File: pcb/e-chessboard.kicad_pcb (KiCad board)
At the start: 2 copper layers, 170 x 170 mm, 55 parts, among them J1 POWER, J2 UART, Q1 BC847, Q2 BC847, SW1 Reset, SW2 Boot, U1 ESP32-WROOM-32U, U2 AOZ1280, U3 NCV7608

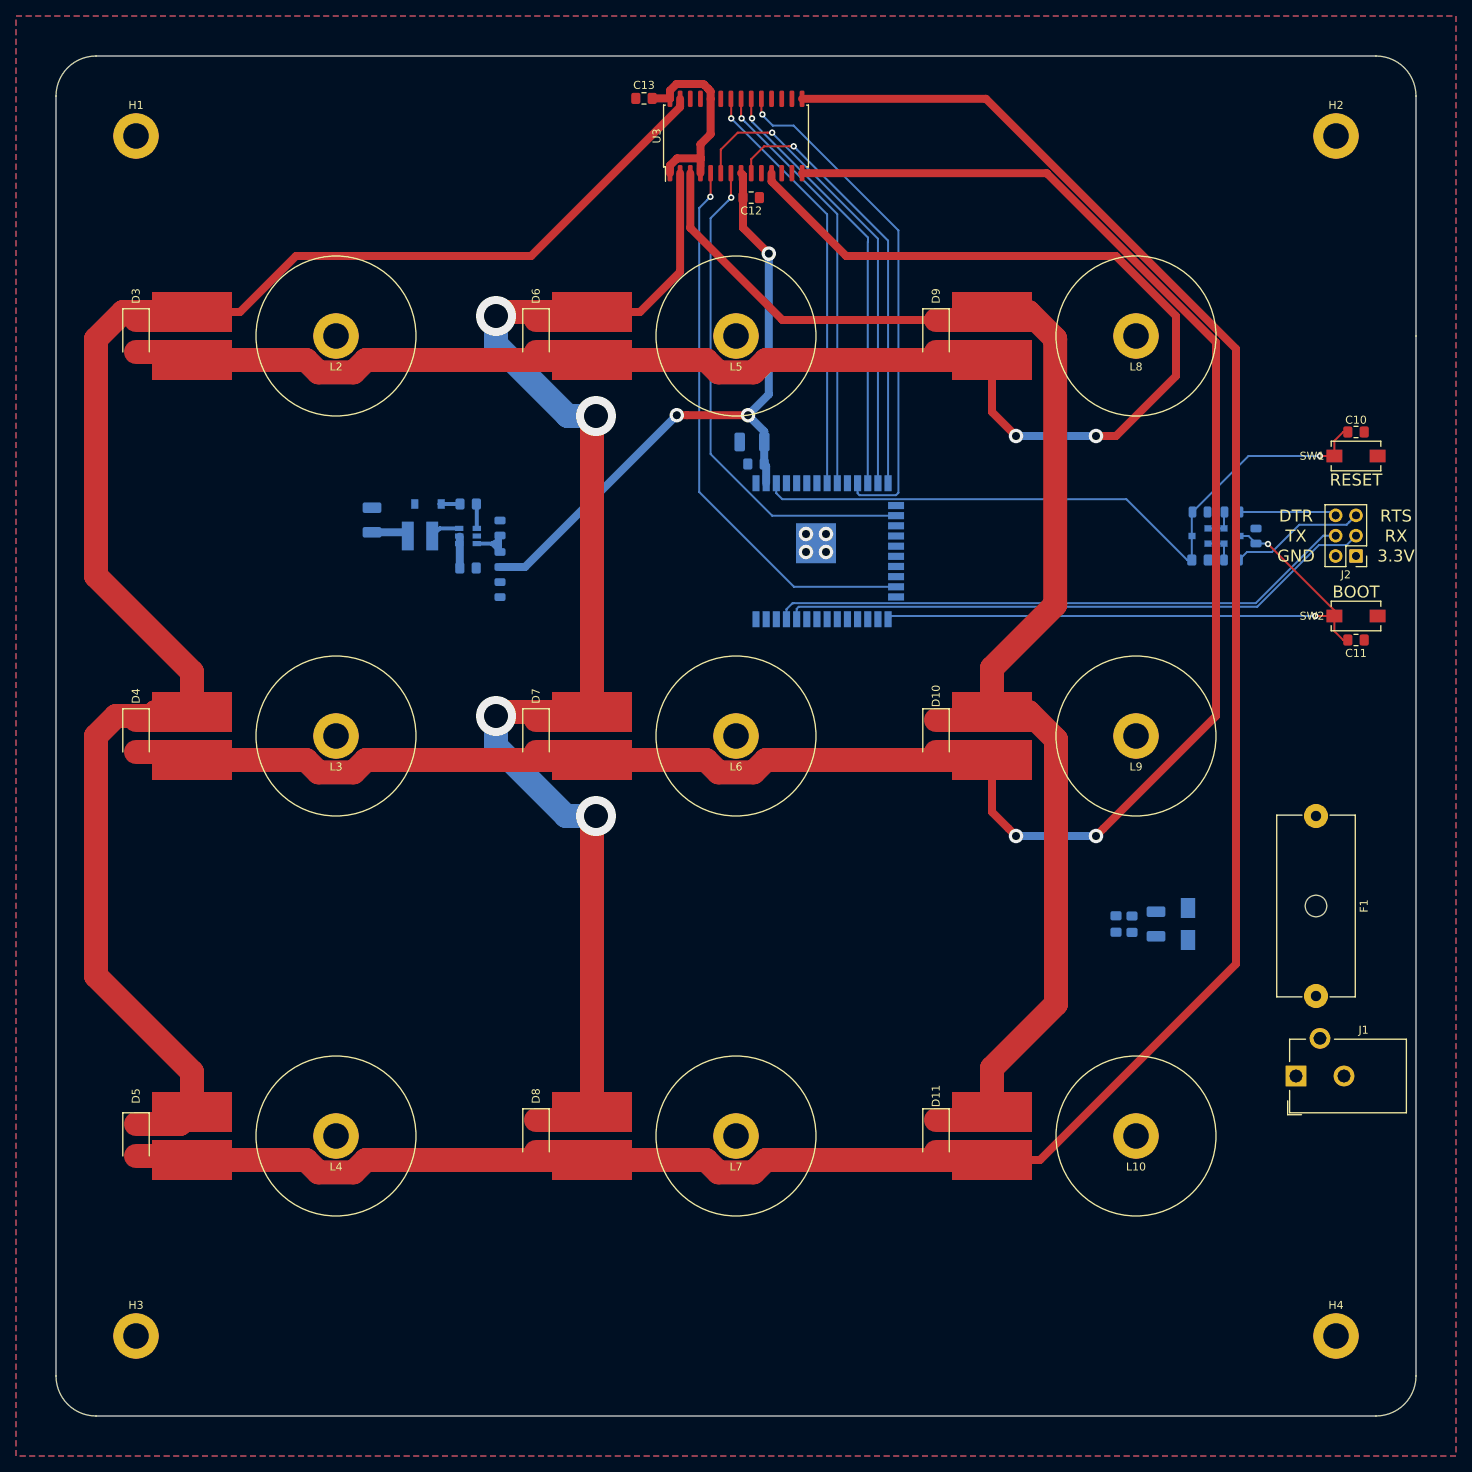
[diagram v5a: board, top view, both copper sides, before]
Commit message: feat(kicad): laying all traces
Laying all missing traces. Next step: via stitching
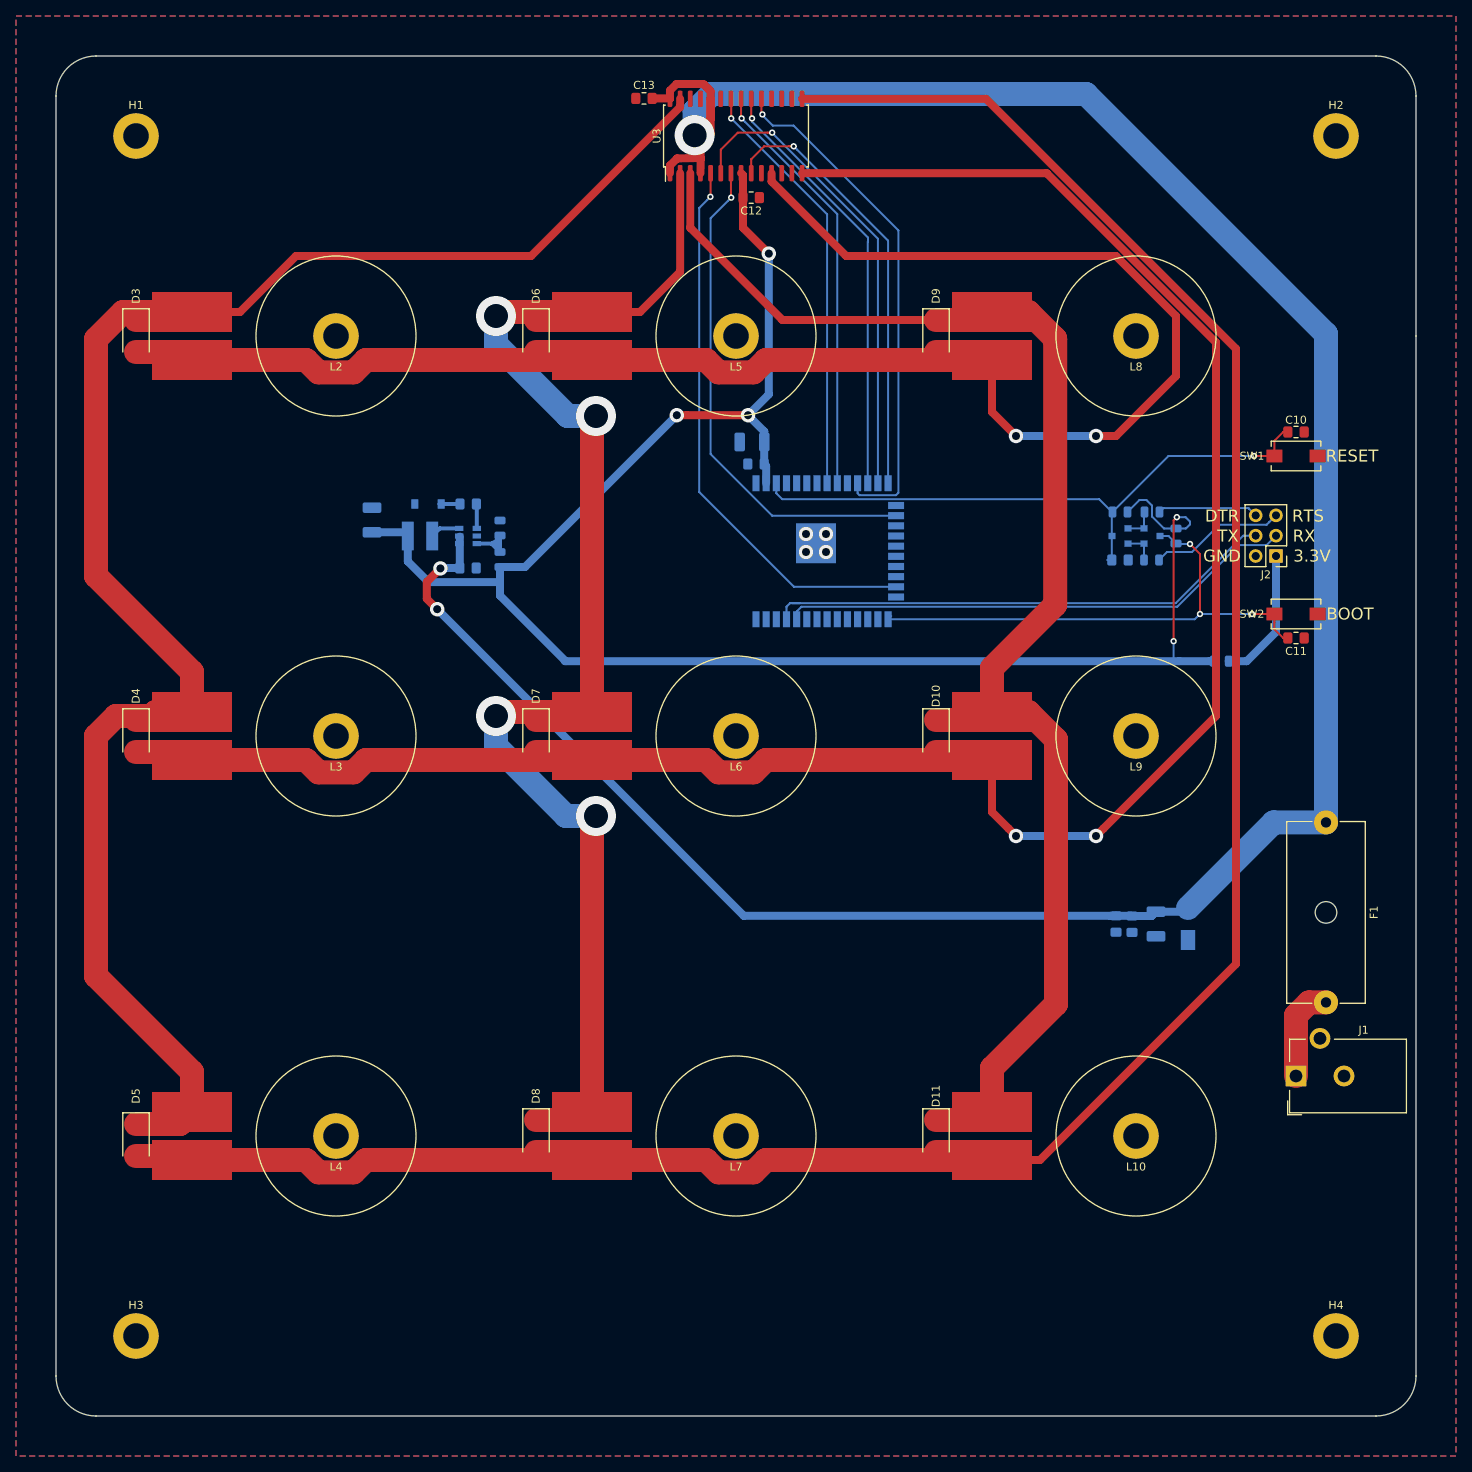
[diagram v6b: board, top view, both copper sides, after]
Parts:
- moved R7 90.6 mm to (195.7, 125.7), turned to 180 degrees
- moved C9 10.0 mm to (183.0, 113.0)
- moved J2 10.0 mm to (202.5, 112.5)
- moved Q1 10.0 mm to (183.0, 110.0)
- moved Q2 10.0 mm to (187.0, 110.0)
- moved R1 10.0 mm to (187.0, 107.0)
- moved R2 10.0 mm to (186.9, 113.0)
- moved R5 10.0 mm to (183.0, 107.0)
- moved R6 10.0 mm to (190.0, 110.0)
- moved C11 7.50 mm to (205.0, 122.8)
- moved SW2 7.50 mm to (205.0, 119.8)
- moved C10 7.50 mm to (205.0, 97.0)
- moved SW1 7.50 mm to (205.0, 100.0)
- moved F1 1.48 mm to (208.8, 145.8)
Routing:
- net +12V: track 33.0 -> 338.4 mm, vias 0 -> 3
- net +3V3: track 85.7 -> 229.1 mm, vias 3 -> 5
- net Net-(J2-Pad1): track 0.00 -> 16.9 mm
- net Net-(F1-Pad2): track 0.00 -> 12.0 mm
- net UART_RX: track 75.0 -> 64.8 mm
- net EN: track 87.3 -> 78.2 mm
- net UART_TX: track 73.7 -> 64.9 mm
- net IO0: track 76.3 -> 71.3 mm, vias 2 -> 3

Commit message: feat(kicad): adding via stictes
Adding 0.8/0.4 via stitching.
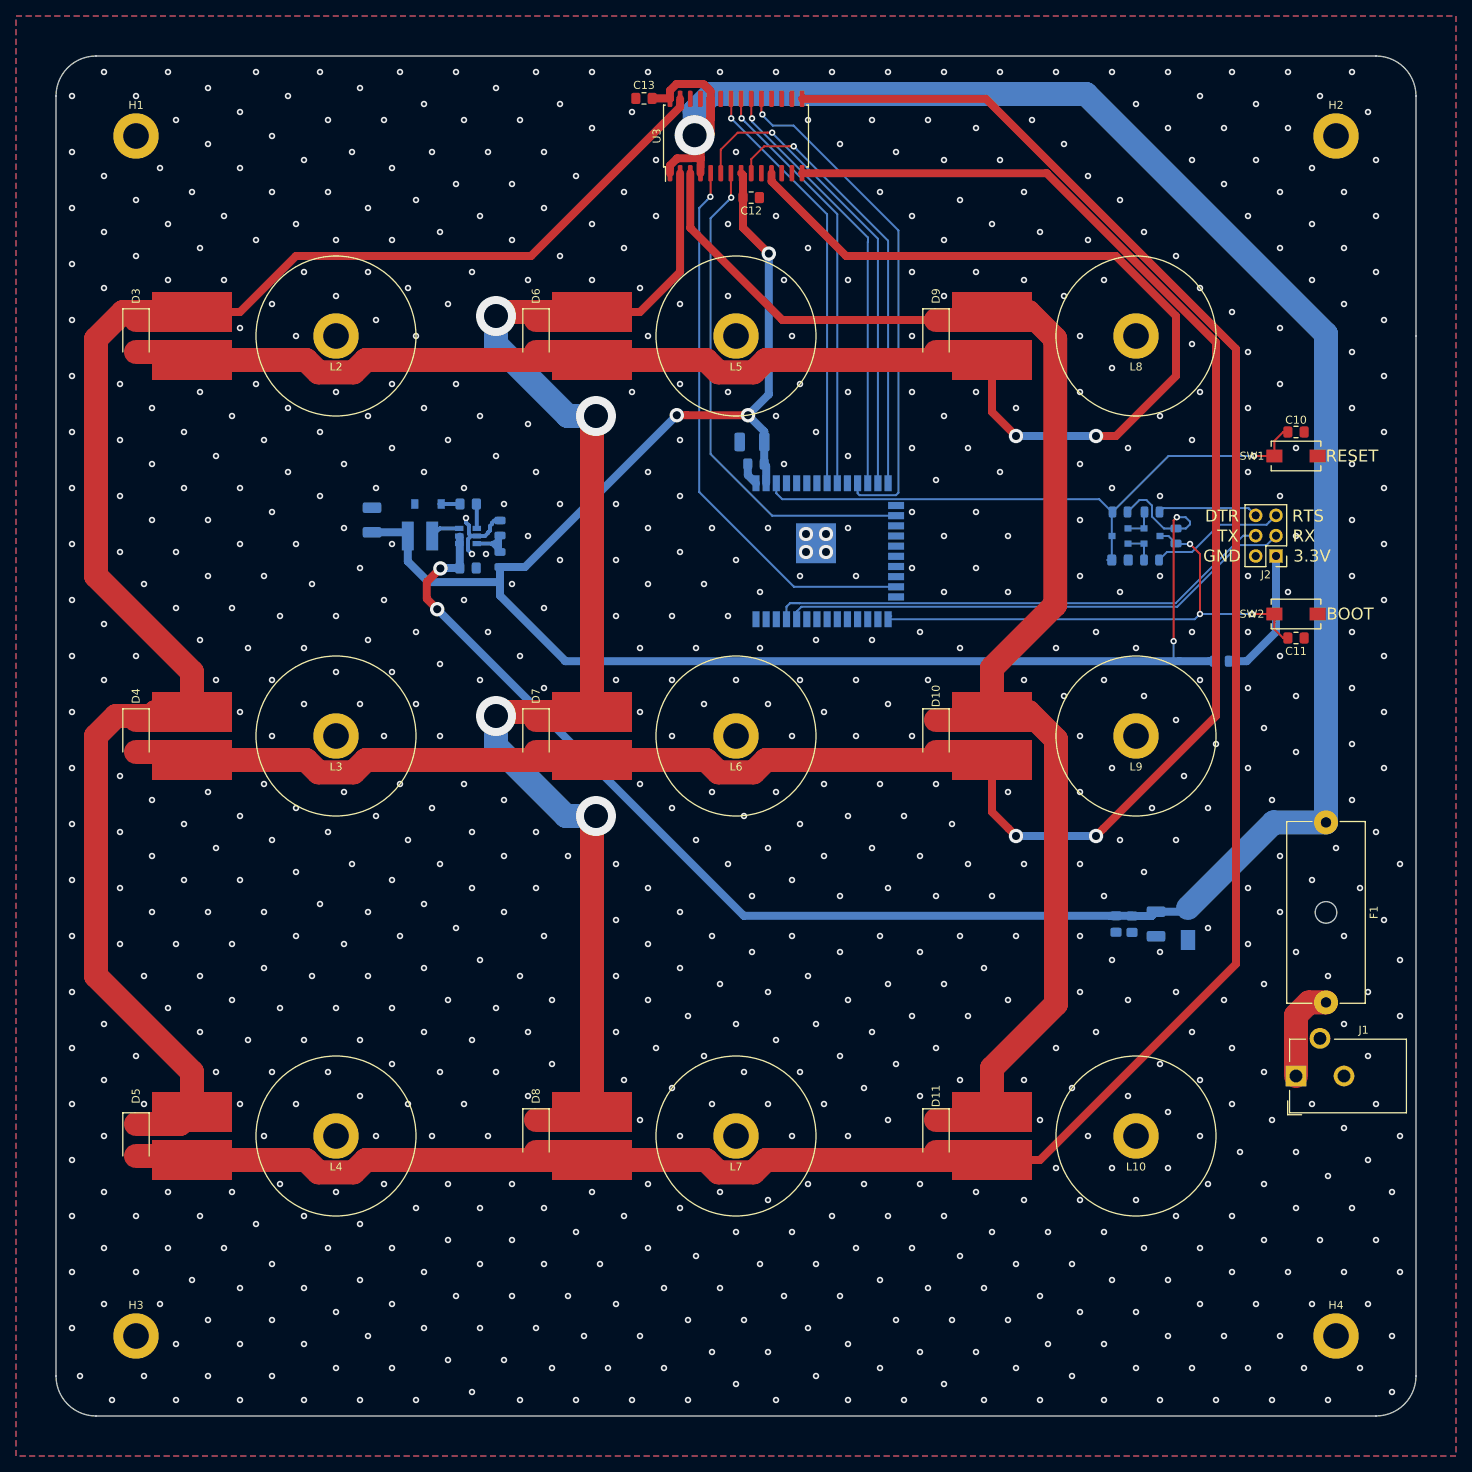
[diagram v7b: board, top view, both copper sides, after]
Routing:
- net GND: track 0.00 -> 14.0 mm, vias 4 -> 808
